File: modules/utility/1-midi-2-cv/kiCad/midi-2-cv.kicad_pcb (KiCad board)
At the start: 2 copper layers, 101 x 110 mm, 163 parts, among them J1 DIN-6, Q1 BC848, Q2 BC848, Q3 BC848, Q4 BC848, SW1 ON-OFF-ON, U1 6N135, U10 MCP4728, U2 YAAJ_WeAct_BlackPill_Part_Like, U3 MCP4728, U4 TL074, U5 MCP4728, U6 TL074, U7 L7805, U8 TL074, U9 TL074

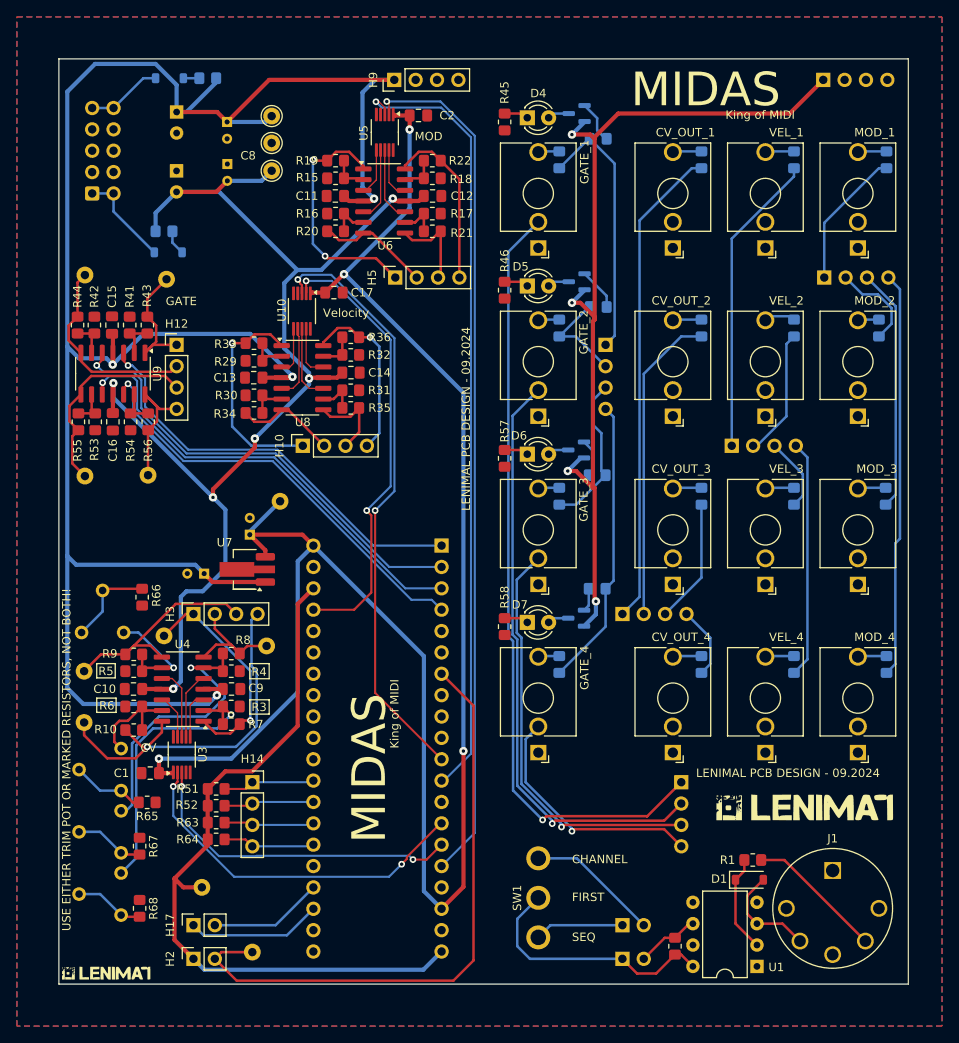
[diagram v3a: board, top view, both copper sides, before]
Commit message: Midi 2 CV (Midas) Rework; Delay (Richochet) Rework. Programming, backups for WeAct CV
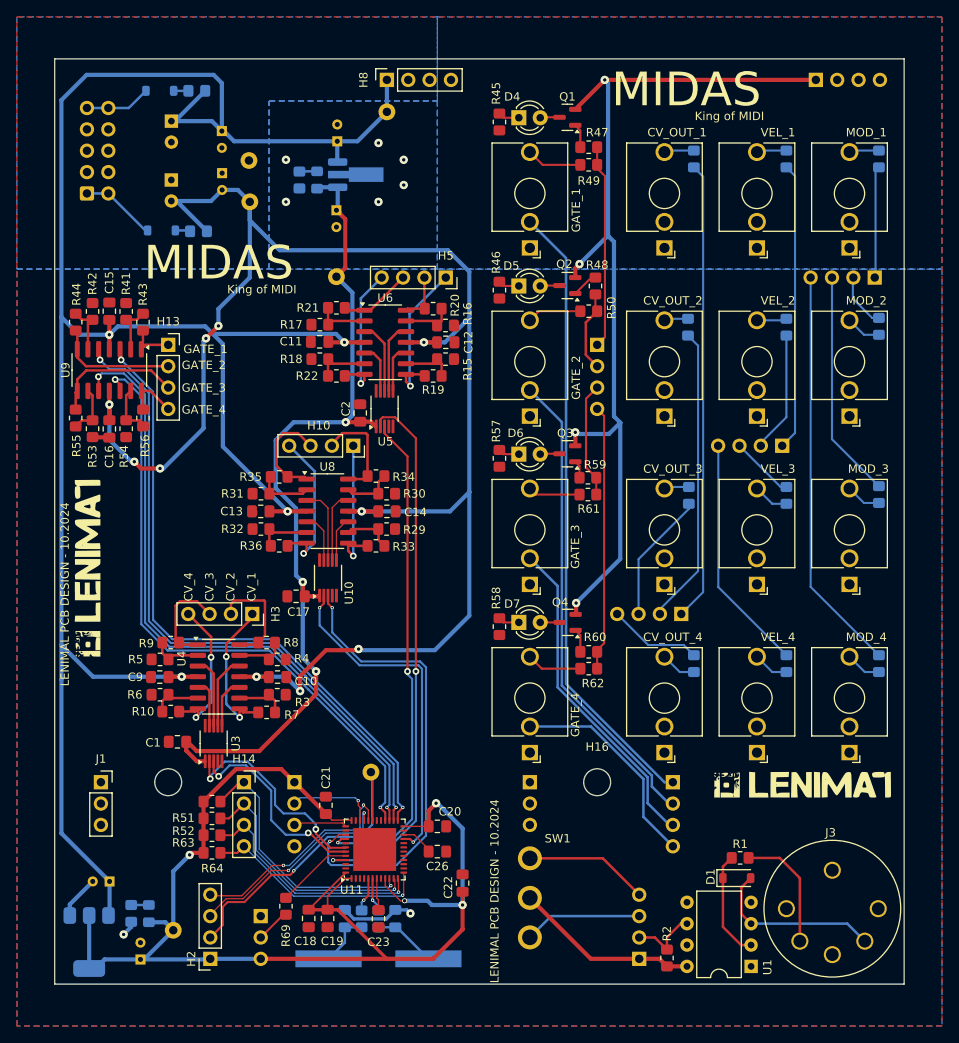
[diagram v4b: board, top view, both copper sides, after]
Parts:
- removed the G*** at (138.8, 139.0)
- removed the G*** at (55.7, 158.7)
- removed the G*** at (55.6, 158.7)
- removed the G*** at (138.6, 139.0)
- removed R65, R66, R67, R68: 6K8, Resistor_SMD:R_0805_2012Metric_Pad1.20x1.40mm_HandSolder
- removed RV1, RV2, RV3, RV4: 20K, Potentiometer_THT:Potentiometer_Piher_PT-6-V_Vertical
- removed TP10: GATE_1_OUT, Connector_Pin:Pin_D1.0mm_L10.0mm
- removed TP11: CV_2_OUT, Connector_Pin:Pin_D1.0mm_L10.0mm
- removed TP12: CV_1_OUT, Connector_Pin:Pin_D1.0mm_L10.0mm
- removed TP13: CV_3_OUT, Connector_Pin:Pin_D1.0mm_L10.0mm
- removed TP14: CV_4_OUT, Connector_Pin:Pin_D1.0mm_L10.0mm
- removed TP7: GATE_3_OUT, Connector_Pin:Pin_D1.0mm_L10.0mm
- removed TP8: GATE_4_OUT, Connector_Pin:Pin_D1.0mm_L10.0mm
- removed TP9: GATE_2_OUT, Connector_Pin:Pin_D1.0mm_L10.0mm
- added C18: 100nF, Capacitor_SMD:C_0805_2012Metric_Pad1.18x1.45mm_HandSolder, F.Cu at (79.7, 152.2)
- added C19: 100nF, Capacitor_SMD:C_0805_2012Metric_Pad1.18x1.45mm_HandSolder, F.Cu at (82.0, 152.2)
- added C20: 100nF, Capacitor_SMD:C_0805_2012Metric_Pad1.18x1.45mm_HandSolder, F.Cu at (95.0, 141.2)
- added C21: 100nF, Capacitor_SMD:C_0805_2012Metric_Pad1.18x1.45mm_HandSolder, F.Cu at (81.8, 138.8)
- added C22: 10uF, Capacitor_SMD:C_0805_2012Metric_Pad1.18x1.45mm_HandSolder, F.Cu at (98.0, 148.0)
- added C23: 100nF, Capacitor_SMD:C_0805_2012Metric_Pad1.18x1.45mm_HandSolder, F.Cu at (88.0, 152.2)
- added C24: 10pF, Capacitor_SMD:C_0805_2012Metric_Pad1.18x1.45mm_HandSolder, B.Cu at (90.0, 152.2)
- added C25: 10pF, Capacitor_SMD:C_0805_2012Metric_Pad1.18x1.45mm_HandSolder, B.Cu at (84.0, 152.2)
- added C26: 2.2uF, Capacitor_SMD:C_0805_2012Metric_Pad1.18x1.45mm_HandSolder, F.Cu at (95.0, 144.2)
- added C27: 10uF, Capacitor_THT:CP_Radial_D4.0mm_P2.00mm, B.Cu at (56.0, 147.8)
- added C28: 10uF, Capacitor_THT:CP_Radial_D4.0mm_P2.00mm, B.Cu at (59.7, 157.1)
- added D8: LED, LED_SMD:LED_0805_2012Metric_Pad1.15x1.40mm_HandSolder, B.Cu at (80.7, 64.4)
- added D9: LED, LED_SMD:LED_0805_2012Metric_Pad1.15x1.40mm_HandSolder, B.Cu at (60.7, 151.6)
- added G***: LOGO, Synth:lenimal_logo_full, F.Cu at (53.4, 110.5)
- added G***: LOGO, Synth:lenimal_logo_full, F.Cu at (138.5, 136.3)
- added G***: LOGO, Synth:lenimal_logo_full, B.Cu at (53.3, 110.4)
- added G***: LOGO, Synth:lenimal_logo_full, B.Cu at (138.6, 136.2)
- added H18: PinHeader_01x04, Synth:PinHeader_1x04_P2.54mm_Vertical, B.Cu at (78.0, 136.0)
- added J2: BOOT_RUN, Connector_PinHeader_2.54mm:PinHeader_1x03_P2.54mm_Vertical, B.Cu at (74.0, 151.9)
- added J3: CONN6_SD-50BV_CUD, Synth:SD-50BV (DIN5), F.Cu at (142.0, 151.0)
- added J4: Conn_01x03, Connector_PinHeader_2.54mm:PinHeader_1x03_P2.54mm_Vertical, B.Cu at (106.0, 136.0)
- added R69: 10K, Resistor_SMD:R_0805_2012Metric_Pad1.20x1.40mm_HandSolder, F.Cu at (77.0, 150.8)
- added R70: 2K, Resistor_SMD:R_0805_2012Metric_Pad1.20x1.40mm_HandSolder, B.Cu at (78.6, 64.4)
- added R71: 2K, Resistor_SMD:R_0805_2012Metric_Pad1.20x1.40mm_HandSolder, B.Cu at (58.6, 151.6)
- added R72: 10R, Resistor_SMD:R_0805_2012Metric_Pad1.20x1.40mm_HandSolder, B.Cu at (86.0, 152.2)
- added R73: 10R, Resistor_SMD:R_0805_2012Metric_Pad1.20x1.40mm_HandSolder, B.Cu at (88.0, 152.2)
- added U11: STM32F401CCUx, Package_DFN_QFN:QFN-48-1EP_7x7mm_P0.5mm_EP5.1x5.1mm, F.Cu at (87.5, 144.0)
- added Y1: 20MHZ, Crystal:Crystal_SMD_HC49-SD_HandSoldering, B.Cu at (88.0, 157.0)
- C3, C6: value 0.1uF -> 10uF
- H1: value PinHeader_01x02 -> PinHeader_01x04; footprint Synth:PinHeader_1x02_P2.54mm_Vertical -> Synth:PinHeader_1x04_P2.54mm_Vertical
- H12, H9, TP1, TP2, TP3: moved to B.Cu
- H13, H8, Q1, Q2, Q3, Q4, R47, R48, R49, R50, R59, R60, R61, R62: moved to F.Cu
- H16: value PinHeader_01x02 -> MountingHole; footprint Synth:PinHeader_1x02_P2.54mm_Vertical -> MountingHole:MountingHole_3.2mm_M3; moved to F.Cu
- H17: value PinSocket_01x02 -> MountingHole; footprint Synth:PinSocket_1x02_P2.54mm_Vertical -> MountingHole:MountingHole_3.2mm_M3
- H2: value PinSocket_01x02 -> PinSocket_01x04; footprint Synth:PinSocket_1x02_P2.54mm_Vertical -> Synth:PinSocket_1x04_P2.54mm_Vertical
- J1: value DIN-6 -> Conn_01x03; footprint Synth:MIDI_DIN5-SD-60BV -> Connector_PinSocket_2.54mm:PinSocket_1x03_P2.54mm_Vertical
- U2: value YAAJ_WeAct_BlackPill_Part_Like -> L78L05_SOT89; footprint stm32:YAAJ_WeAct_BlackPill_2 -> Package_TO_SOT_SMD:SOT-89-3_Handsoldering
- U7: value L7805 -> AMS1117-3.3; footprint Package_TO_SOT_SMD:SOT-89-3_Handsoldering -> Package_TO_SOT_SMD:SOT-223-3_TabPin2; moved to B.Cu
- moved J1 88.3 mm to (55.0, 136.0)
- moved C3 53.8 mm to (83.1, 59.8), turned to 90 degrees
- moved H13 52.0 mm to (63.0, 84.0), turned to 0 degrees
- moved H8 51.9 mm to (89.0, 52.5), turned to 90 degrees
- moved H9 50.1 mm to (140.0, 52.5), turned to -90 degrees
- moved H12 50.0 mm to (114.0, 84.0), turned to 180 degrees
- moved U7 48.0 mm to (53.6, 155.0), turned to -90 degrees
- moved U2 45.2 mm to (85.6, 63.8), turned to 0 degrees
- moved C6 39.9 mm to (83.0, 68.0), turned to -90 degrees
- moved C17 36.4 mm to (78.2, 113.9), turned to 0 degrees
- moved C2 36.0 mm to (85.8, 92.1), turned to -90 degrees
- moved U5 32.9 mm to (88.7, 91.6), turned to 90 degrees
- moved U10 31.9 mm to (82.0, 111.7), turned to 90 degrees
- moved R33 28.1 mm to (87.7, 107.9)
- moved R19 28.1 mm to (94.5, 87.7)
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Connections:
- H14 pad 1: /gate_out/GATE_1_CALLBACK -> /PA0
- H14 pad 2: /gate_out/GATE_2_CALLBACK -> /PA1
- H14 pad 3: /gate_out/GATE_3_CALLBACK -> /PA2
- H14 pad 4: /gate_out/GATE_4_CALLBACK -> /PA3
- H2 pad 2: Net-(H2B-Pin_2) -> /RX
- J1 pad 1: unconnected-(J1-Pad1) -> GNDREF
- J1 pad 2: Net-(J1-Pad2) -> GNDREF
- R1 pad 2: Net-(J1-Pad2) -> Net-(J3-Pad2)
- R10 pad 1: Net-(U4D--) -> Net-(U4B--)
- R15 pad 2: Net-(U6A--) -> Net-(U6C--)
- R16 pad 2: Net-(U6B--) -> Net-(U6D--)
- R17 pad 2: Net-(U6C--) -> Net-(U6A--)
- R18 pad 2: Net-(U6D--) -> Net-(U6B--)
- R19 pad 1: Net-(U6A--) -> Net-(U6C--)
- R20 pad 1: Net-(U6B--) -> Net-(U6D--)
- R21 pad 1: Net-(U6C--) -> Net-(U6A--)
- R22 pad 1: Net-(U6D--) -> Net-(U6B--)
- R29 pad 2: Net-(U8A--) -> Net-(U8C--)
- R3 pad 2: Net-(U4A--) -> Net-(U4C--)
- R30 pad 2: Net-(U8B--) -> Net-(U8D--)
- R31 pad 2: Net-(U8C--) -> Net-(U8A--)
- R32 pad 2: Net-(U8D--) -> Net-(U8B--)
- R33 pad 1: Net-(U8A--) -> Net-(U8C--)
- R34 pad 1: Net-(U8B--) -> Net-(U8D--)
- R35 pad 1: Net-(U8C--) -> Net-(U8A--)
- R36 pad 1: Net-(U8D--) -> Net-(U8B--)
- R4 pad 2: Net-(U4B--) -> Net-(U4D--)
- R43 pad 2: Net-(H12A-Pin_1) -> Net-(H13A-Pin_1)
- R44 pad 2: Net-(H12B-Pin_2) -> Net-(H13B-Pin_2)
- R47 pad 1: Net-(H13A-Pin_1) -> Net-(H12A-Pin_1)
- R48 pad 1: Net-(H13B-Pin_2) -> Net-(H12B-Pin_2)
- R49 pad 1: Net-(H13A-Pin_1) -> Net-(H12A-Pin_1)
- R5 pad 2: Net-(U4C--) -> Net-(U4A--)
- R50 pad 1: Net-(H13B-Pin_2) -> Net-(H12B-Pin_2)
- R51 pad 1: /gate_out/GATE_1_CALLBACK -> /PA0
- R52 pad 1: /gate_out/GATE_2_CALLBACK -> /PA1
- R55 pad 2: Net-(H12C-Pin_3) -> Net-(H13C-Pin_3)
- R56 pad 2: Net-(H12D-Pin_4) -> Net-(H13D-Pin_4)
- R59 pad 1: Net-(H13C-Pin_3) -> Net-(H12C-Pin_3)
- R6 pad 2: Net-(U4D--) -> Net-(U4B--)
- R60 pad 1: Net-(H13D-Pin_4) -> Net-(H12D-Pin_4)
- R61 pad 1: Net-(H13C-Pin_3) -> Net-(H12C-Pin_3)
- R62 pad 1: Net-(H13D-Pin_4) -> Net-(H12D-Pin_4)
- R63 pad 1: /gate_out/GATE_3_CALLBACK -> /PA2
- R64 pad 1: /gate_out/GATE_4_CALLBACK -> /PA3
- R7 pad 1: Net-(U4A--) -> Net-(U4C--)
- R8 pad 1: Net-(U4B--) -> Net-(U4D--)
- R9 pad 1: Net-(U4C--) -> Net-(U4A--)
- SW1 pad 1: Net-(H16A-Pin_1) -> Net-(H1C-Pin_3)
- SW1 pad 3: Net-(H16B-Pin_2) -> Net-(H1D-Pin_4)
- TP6 pad 1: Net-(H2B-Pin_2) -> /RX
- U10 pad 2: /mcp4728_velocity-out/SCL -> /PB10-vel-scl
- U10 pad 3: /mcp4728_velocity-out/SDA -> /PB3-vel-sda
- U2 pad 1: /gate_out/GATE_IN_1 -> +5V
- U2 pad 2: /gate_out/GATE_IN_2 -> GNDREF
- U2 pad 3: /gate_out/GATE_IN_3 -> +12V
- U3 pad 2: /mcp4728_cv-out/SCL -> /PB6-cv-scl
- U3 pad 3: /mcp4728_cv-out/SDA -> /PB7-cv-sda
- U4 pad 1: Net-(H3A-Pin_1) -> Net-(H3C-Pin_3)
- U4 pad 10: Net-(U3-VOUTC) -> Net-(U3-VOUTA)
- U4 pad 12: Net-(U3-VOUTD) -> Net-(U3-VOUTB)
- U4 pad 14: Net-(H3D-Pin_4) -> Net-(H3B-Pin_2)
- U4 pad 3: Net-(U3-VOUTA) -> Net-(U3-VOUTC)
- U4 pad 5: Net-(U3-VOUTB) -> Net-(U3-VOUTD)
- U4 pad 7: Net-(H3B-Pin_2) -> Net-(H3D-Pin_4)
- U4 pad 8: Net-(H3C-Pin_3) -> Net-(H3A-Pin_1)
- U5 pad 2: /mcp4728_mod-wheel-out/SCL -> /PB8-mod-scl
- U5 pad 3: /mcp4728_mod-wheel-out/SDA -> /PB4-mod-sda
- U6 pad 1: Net-(H5A-Pin_1) -> Net-(H5C-Pin_3)
- U6 pad 10: Net-(U5-VOUTC) -> Net-(U5-VOUTA)
- U6 pad 12: Net-(U5-VOUTD) -> Net-(U5-VOUTB)
- U6 pad 14: Net-(H5D-Pin_4) -> Net-(H5B-Pin_2)
- U6 pad 3: Net-(U5-VOUTA) -> Net-(U5-VOUTC)
- U6 pad 5: Net-(U5-VOUTB) -> Net-(U5-VOUTD)
- U6 pad 7: Net-(H5B-Pin_2) -> Net-(H5D-Pin_4)
- U6 pad 8: Net-(H5C-Pin_3) -> Net-(H5A-Pin_1)
- U7 pad 1: +12V -> GNDREF
- U7 pad 2: GNDREF -> +3.3V
- U7 pad 3: +5V -> +12V
- U8 pad 1: Net-(H10A-Pin_1) -> Net-(H10C-Pin_3)
- U8 pad 10: Net-(U10-VOUTC) -> Net-(U10-VOUTA)
- U8 pad 12: Net-(U10-VOUTD) -> Net-(U10-VOUTB)
- U8 pad 14: Net-(H10D-Pin_4) -> Net-(H10B-Pin_2)
- U8 pad 3: Net-(U10-VOUTA) -> Net-(U10-VOUTC)
- U8 pad 5: Net-(U10-VOUTB) -> Net-(U10-VOUTD)
- U8 pad 7: Net-(H10B-Pin_2) -> Net-(H10D-Pin_4)
- U8 pad 8: Net-(H10C-Pin_3) -> Net-(H10A-Pin_1)
- U9 pad 1: Net-(H12A-Pin_1) -> Net-(H13A-Pin_1)
- U9 pad 14: Net-(H12D-Pin_4) -> Net-(H13D-Pin_4)
- U9 pad 7: Net-(H12B-Pin_2) -> Net-(H13B-Pin_2)
- U9 pad 8: Net-(H12C-Pin_3) -> Net-(H13C-Pin_3)
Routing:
- net +5V: track 219.0 -> 103.7 mm, vias 4 -> 3
- net /mcp4728_mod-wheel-out/SCL: track 102.3 -> 0.00 mm, vias 1 -> 0
- net /mcp4728_mod-wheel-out/SDA: track 93.0 -> 0.00 mm, vias 1 -> 0
- net Net-(H2B-Pin_2): track 73.3 -> 0.00 mm
- net /mcp4728_velocity-out/SDA: track 71.0 -> 0.00 mm, vias 2 -> 0
- net /PB8-mod-scl: track 0.00 -> 65.0 mm, vias 0 -> 2
- net +3.3V: track 118.8 -> 181.0 mm, vias 0 -> 4
- net /PB4-mod-sda: track 0.00 -> 59.2 mm, vias 0 -> 2
- net /PB3-vel-sda: track 0.00 -> 55.5 mm, vias 0 -> 2
- net -12V: track 145.9 -> 201.4 mm, vias 6 -> 10
- net /mcp4728_velocity-out/SCL: track 53.6 -> 0.00 mm, vias 2 -> 0
- net /mcp4728_cv-out/SCL: track 43.1 -> 0.00 mm, vias 2 -> 0
- net /PB10-vel-scl: track 0.00 -> 40.4 mm, vias 0 -> 2
- net /mcp4728_cv-out/SDA: track 39.2 -> 0.00 mm, vias 2 -> 0
- net /RX: track 0.00 -> 38.2 mm, vias 0 -> 1
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- added copper zone on B.Cu, net GNDREF
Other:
- board text added: "3.3V"
- board text added: "CV_1"
- board text added: "CV_2"
- board text added: "CV_3"
- board text added: "CV_4"
- board text added: "GATE_1"
- board text added: "GATE_2"
- board text added: "GATE_3"
- board text added: "GATE_4"
- board text added: "LENIMAL PCB DESIGN - 10.2024"
- board text added: "Mod wheel"
- board text added: "PROG"
- board text added: "RUN"
- board text added: "SWD_CLK"
- board text added: "SWD_IO"
- board text removed: "CH.1"
- board text removed: "CH.2"
- board text removed: "CH.3"
- board text removed: "CH.4"
- board text removed: "CHANNEL"
- board text removed: "CV"
- board text removed: "Channel 1"
- board text removed: "Channel 2"
- board text removed: "Channel 3"
- board text removed: "Channel 4"
- board text removed: "FIRST"
- board text removed: "GATE"
- board text removed: "GATE.1"
- board text removed: "GATE.2"
- board text removed: "GATE.3"
- board text removed: "GATE.4"
- board text removed: "LENIMAL PCB DESIGN - 09.2024"
- board text removed: "MIDI_IN"
- board text removed: "MOD"
- board text removed: "SEQ"
- board text removed: "USB SIDE"
- board text removed: "USE EITHER TRIM POT OR MARKED RESISTORS, NOT BOTH!"

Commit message: finish up PCB finals for run-2, continue on C code for midas/sequencer
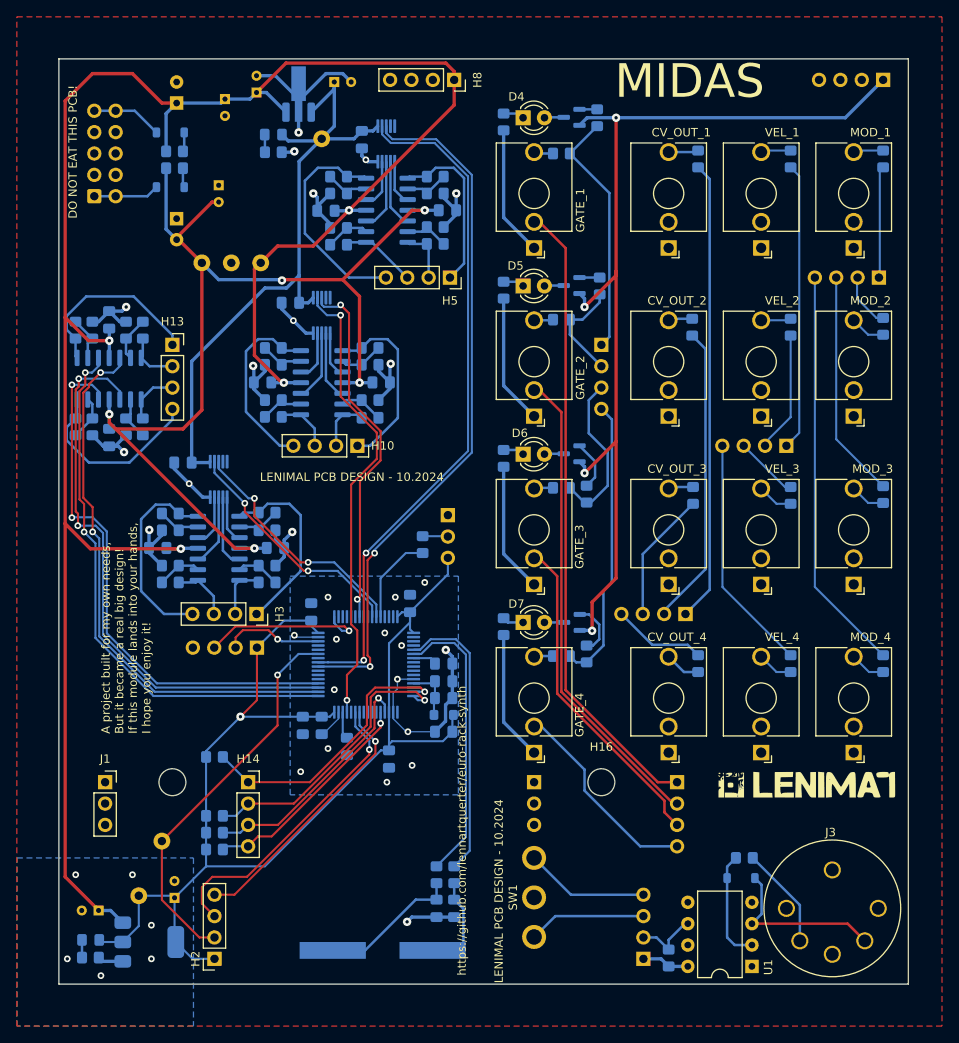
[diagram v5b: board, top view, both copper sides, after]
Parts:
- removed C18, C19, C20, C21, C23: 100nF, Capacitor_SMD:C_0805_2012Metric_Pad1.18x1.45mm_HandSolder
- removed C22: 10uF, Capacitor_SMD:C_0805_2012Metric_Pad1.18x1.45mm_HandSolder
- removed C24, C25: 10pF, Capacitor_SMD:C_0805_2012Metric_Pad1.18x1.45mm_HandSolder
- removed C26: 2.2uF, Capacitor_SMD:C_0805_2012Metric_Pad1.18x1.45mm_HandSolder
- removed the G*** at (53.4, 110.5)
- removed the G*** at (53.3, 110.4)
- removed H18: PinHeader_01x04, Synth:PinHeader_1x04_P2.54mm_Vertical
- removed J2: BOOT_RUN, Connector_PinHeader_2.54mm:PinHeader_1x03_P2.54mm_Vertical
- removed R69: 10K, Resistor_SMD:R_0805_2012Metric_Pad1.20x1.40mm_HandSolder
- removed R72, R73: 10R, Resistor_SMD:R_0805_2012Metric_Pad1.20x1.40mm_HandSolder
- removed Y1: 20MHZ, Crystal:Crystal_SMD_HC49-SD_HandSoldering
- added C29: 100nF, Capacitor_SMD:C_0805_2012Metric_Pad1.18x1.45mm_HandSolder, B.Cu at (81.2, 129.2)
- added C30: 100nF, Capacitor_SMD:C_0805_2012Metric_Pad1.18x1.45mm_HandSolder, B.Cu at (80.0, 115.8)
- added C31: 100nF, Capacitor_SMD:C_0805_2012Metric_Pad1.18x1.45mm_HandSolder, B.Cu at (89.2, 133.2)
- added C32: 100nF, Capacitor_SMD:C_0805_2012Metric_Pad1.18x1.45mm_HandSolder, B.Cu at (91.8, 114.8)
- added C33: 10uF, Capacitor_SMD:C_0805_2012Metric_Pad1.18x1.45mm_HandSolder, B.Cu at (79.0, 129.2)
- added C34: 100nF, Capacitor_SMD:C_0805_2012Metric_Pad1.18x1.45mm_HandSolder, B.Cu at (95.8, 121.9)
- added C35: 10nF, Capacitor_SMD:C_0805_2012Metric_Pad1.18x1.45mm_HandSolder, B.Cu at (95.8, 124.0)
- added C36: 1uF, Capacitor_SMD:C_0805_2012Metric_Pad1.18x1.45mm_HandSolder, B.Cu at (95.8, 126.0)
- added C37: 1uF, Capacitor_SMD:C_0805_2012Metric_Pad1.18x1.45mm_HandSolder, B.Cu at (95.8, 130.0)
- added C38: 10pF, Capacitor_SMD:C_0805_2012Metric_Pad1.18x1.45mm_HandSolder, B.Cu at (97.0, 151.0)
- added C39: 10pF, Capacitor_SMD:C_0805_2012Metric_Pad1.18x1.45mm_HandSolder, B.Cu at (94.9, 151.0)
- added C40: 2.2uF, Capacitor_SMD:C_0805_2012Metric_Pad1.18x1.45mm_HandSolder, B.Cu at (84.2, 131.8)
- added FB1: 120R, Inductor_SMD:L_0805_2012Metric_Pad1.05x1.20mm_HandSolder, B.Cu at (95.8, 128.0)
- added G***: LOGO, Synth:lenimal_logo_full, B.Cu at (86.0, 139.5)
- added J5: BOOT_RUN, Connector_PinHeader_2.54mm:PinHeader_1x03_P2.54mm_Vertical, B.Cu at (96.2, 104.2)
- added J6: Conn_01x04, Connector_PinHeader_2.54mm:PinHeader_1x04_P2.54mm_Vertical, B.Cu at (73.5, 120.0)
- added R65: 10K, Resistor_SMD:R_0805_2012Metric_Pad1.20x1.40mm_HandSolder, B.Cu at (93.2, 107.8)
- added R66: 10R, Resistor_SMD:R_0805_2012Metric_Pad1.20x1.40mm_HandSolder, B.Cu at (97.0, 147.0)
- added R67: 10R, Resistor_SMD:R_0805_2012Metric_Pad1.20x1.40mm_HandSolder, B.Cu at (94.9, 147.0)
- added Y2: 20MHZ, Crystal:Crystal_SMD_HC49-SD_HandSoldering, B.Cu at (88.5, 156.0)
- C1, C10, C11, C12, C13, C14, C15, C16, C17, C2, C9, D1, Q1, Q2, Q3, Q4, R1, R2, R3, R4, R41, R42, R43, R44, R45, R46, R47, R48, R49, R5, R50, R51, R52, R53, R54, R55, R56, R57, R58, R59, R6, R60, R61, R62, R63, R64, U10, U3, U5: moved to B.Cu
- J3: value CONN6_SD-50BV_CUD -> SD-50BV (DIN5)
- R10, R7, R8, R9: value 47K [0.1%] -> 30K [0.1%]; moved to B.Cu
- R15, R16, R17, R18, R29, R30, R31, R32: value 10K [1%] -> 10K [0.1%]; moved to B.Cu
- R19, R20, R21, R22, R33, R34, R35, R36: value 47K [1%] -> 30K [0.1%]; moved to B.Cu
- U11: value STM32F401CCUx -> STM32F411RETx; footprint Package_DFN_QFN:QFN-48-1EP_7x7mm_P0.5mm_EP5.1x5.1mm -> Package_QFP:LQFP-64_10x10mm_P0.5mm; moved to B.Cu
- U4, U6, U8, U9: footprint Package_SO:SOIC-14_3.9x8.7mm_P1.27mm -> Synth:SOIC-14; moved to B.Cu
- moved C17 34.9 mm to (77.5, 79.0)
- moved C1 33.2 mm to (64.8, 98.0)
- moved C2 32.5 mm to (86.0, 59.6), turned to 90 degrees
- moved U5 31.5 mm to (88.9, 60.1), turned to -90 degrees
- moved U3 31.4 mm to (69.0, 100.0), turned to -90 degrees
- moved U10 31.2 mm to (81.2, 80.5), turned to -90 degrees
- moved TP6 26.2 mm to (62.2, 143.0)
- moved R7 23.8 mm to (74.8, 104.0)
- moved R19 23.7 mm to (94.8, 64.0)
- moved R22 23.7 mm to (83.2, 64.0)
- moved R10 23.6 mm to (63.2, 104.0)
- moved R33 23.5 mm to (87.0, 84.4)
- moved R36 23.5 mm to (75.5, 84.4)
- moved TP2 23.4 mm to (74.0, 74.2), turned to 180 degrees
- moved U11 22.0 mm to (86.5, 122.0), turned to 180 degrees
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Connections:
- net /PB4-mod-sda renamed /STM32F411RE/MOD_SDA
- H14 pad 1: /PA0 -> /STM32F411RE/GATE_1_IN
- H14 pad 2: /PA1 -> /STM32F411RE/GATE_2_IN
- H14 pad 3: /PA2 -> /STM32F411RE/GATE_3_IN
- H14 pad 4: /PA3 -> /STM32F411RE/GATE_4_IN
- H2 pad 2: /RX -> /STM32F411RE/MIDI_IN
- H2 pad 3: /MODE_1 -> /STM32F411RE/MODE_SW_1
- H2 pad 4: /MODE_2 -> /STM32F411RE/MODE_SW_2
- R51 pad 1: /PA0 -> /STM32F411RE/GATE_1_IN
- R52 pad 1: /PA1 -> /STM32F411RE/GATE_2_IN
- R63 pad 1: /PA2 -> /STM32F411RE/GATE_3_IN
- R64 pad 1: /PA3 -> /STM32F411RE/GATE_4_IN
- SW1 pad 2: +3.3V -> GNDREF
- TP6 pad 1: /RX -> /STM32F411RE/MIDI_IN
- U10 pad 2: /PB10-vel-scl -> /STM32F411RE/VEL_SCL
- U10 pad 3: /PB3-vel-sda -> /STM32F411RE/VEL_SDA
- U11 pad 10: /PA0 -> unconnected-(U11-PC2-Pad10)
- U11 pad 11: /PA1 -> unconnected-(U11-PC3-Pad11)
- U11 pad 12: /PA2 -> GNDREF
- U11 pad 13: /PA3 -> +3.3VA
- U11 pad 15: unconnected-(U11-PA5-Pad15) -> /STM32F411RE/GATE_1_IN
- U11 pad 16: unconnected-(U11-PA6-Pad16) -> /STM32F411RE/GATE_2_IN
- U11 pad 18: unconnected-(U11-PB0-Pad18) -> GNDREF
- U11 pad 19: unconnected-(U11-PB1-Pad19) -> +3.3V
- U11 pad 20: unconnected-(U11-PB2-Pad20) -> /STM32F411RE/GATE_3_IN
- U11 pad 21: /PB10-vel-scl -> /STM32F411RE/GATE_4_IN
- U11 pad 22: /VCap -> unconnected-(U11-PA6-Pad22)
- U11 pad 23: GNDREF -> unconnected-(U11-PA7-Pad23)
- U11 pad 24: +3.3V -> unconnected-(U11-PC4-Pad24)
- U11 pad 25: /gate_out/GATE_IN_1 -> unconnected-(U11-PC5-Pad25)
- U11 pad 26: /gate_out/GATE_IN_2 -> /STM32F411RE/MODE_SW_2
- U11 pad 27: /gate_out/GATE_IN_3 -> /STM32F411RE/MODE_SW_1
- U11 pad 28: /gate_out/GATE_IN_4 -> unconnected-(U11-PB2-Pad28)
- U11 pad 29: unconnected-(U11-PA8-Pad29) -> /STM32F411RE/VEL_SCL
- U11 pad 30: unconnected-(U11-PA9-Pad30) -> /STM32F411RE/VCap
- U11 pad 31: /RX -> GNDREF
- U11 pad 32: /MODE_2 -> +3.3V
- U11 pad 33: /MODE_1 -> /STM32F411RE/GATE_1_OUT
- U11 pad 34: /SWD_IO -> /STM32F411RE/GATE_2_OUT
- U11 pad 35: GNDREF -> /STM32F411RE/GATE_3_OUT
- U11 pad 36: +3.3V -> /STM32F411RE/GATE_4_OUT
- U11 pad 37: /SWD_CLK -> unconnected-(U11-PC6-Pad37)
- U11 pad 39: /PB3-vel-sda -> unconnected-(U11-PC8-Pad39)
- U11 pad 41: unconnected-(U11-PB5-Pad41) -> /STM32F411RE/MOD_SCL
- U11 pad 42: /PB6-cv-scl -> unconnected-(U11-PA9-Pad42)
- U11 pad 43: /PB7-cv-sda -> /STM32F411RE/MIDI_IN
- U11 pad 44: Net-(U11-BOOT0) -> unconnected-(U11-PA11-Pad44)
- U11 pad 45: /PB8-mod-scl -> unconnected-(U11-PA12-Pad45)
- U11 pad 46: unconnected-(U11-PB9-Pad46) -> /STM32F411RE/SWD_IO
- U11 pad 49: GNDREF -> /STM32F411RE/SWD_CLK
- U11 pad 5: /HSC_IN -> /STM32F411RE/HSC_IN
- U11 pad 6: /HSC_OUT -> /STM32F411RE/HSC_OUT
- U11 pad 7: /NRST -> /STM32F411RE/NRST
- U11 pad 8: GNDREF -> unconnected-(U11-PC0-Pad8)
- U11 pad 9: +3.3V -> unconnected-(U11-PC1-Pad9)
- U3 pad 2: /PB6-cv-scl -> /STM32F411RE/CV_SCL
- U3 pad 3: /PB7-cv-sda -> /STM32F411RE/CV_SDA
- U5 pad 2: /PB8-mod-scl -> /STM32F411RE/MOD_SCL
- U9 pad 10: /gate_out/GATE_IN_3 -> /STM32F411RE/GATE_3_OUT
- U9 pad 12: /gate_out/GATE_IN_4 -> /STM32F411RE/GATE_4_OUT
- U9 pad 3: /gate_out/GATE_IN_1 -> /STM32F411RE/GATE_1_OUT
- U9 pad 5: /gate_out/GATE_IN_2 -> /STM32F411RE/GATE_2_OUT
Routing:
- net GNDREF: track 22.3 -> 195.7 mm, vias 8 -> 35
- net /STM32F411RE/MOD_SCL: track 0.00 -> 81.5 mm, vias 0 -> 2
- net /gate_out/GATE_IN_2: track 79.0 -> 0.00 mm, vias 2 -> 0
- net /gate_out/GATE_IN_3: track 78.5 -> 0.00 mm, vias 2 -> 0
- net /gate_out/GATE_IN_1: track 77.3 -> 0.00 mm, vias 2 -> 0
- net /gate_out/GATE_IN_4: track 75.6 -> 0.00 mm, vias 2 -> 0
- net -12V: track 201.4 -> 131.2 mm, vias 10 -> 5
- net /STM32F411RE/GATE_3_OUT: track 0.00 -> 67.9 mm, vias 0 -> 2
- net /STM32F411RE/GATE_2_OUT: track 0.00 -> 65.3 mm, vias 0 -> 2
- net /PB8-mod-scl: track 65.0 -> 0.00 mm, vias 2 -> 0
- net /STM32F411RE/GATE_1_OUT: track 0.00 -> 64.8 mm, vias 0 -> 2
- net /STM32F411RE/GATE_4_OUT: track 0.00 -> 64.8 mm, vias 0 -> 2
- net /PB3-vel-sda: track 55.5 -> 0.00 mm, vias 2 -> 0
- net /STM32F411RE/VEL_SCL: track 0.00 -> 55.2 mm, vias 0 -> 2
- net /STM32F411RE/MIDI_IN: track 0.00 -> 46.4 mm, vias 0 -> 1
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- removed copper zone on B.Cu, net (none)
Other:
- board text added: "20MHZ"
- board text added: "A project built for my own needs, But it became a real big design! If this module lands into your hands, I hope you enjoy it!"
- board text added: "CLK"
- board text added: "DO NOT EAT THIS PCB!"
- board text added: "IO"
- board text added: "MIDI_IN"
- board text added: "PWR_3V"
- board text added: "PWR_5V"
- board text added: "STM32 F411 RET7"
- board text added: "TL074"
- board text added: "https://github.com/lennartquerter/euro-rack-synth"
- board text removed: "3.3V"
- board text removed: "CV_1"
- board text removed: "CV_2"
- board text removed: "CV_3"
- board text removed: "CV_4"
- board text removed: "GATE_1"
- board text removed: "GATE_2"
- board text removed: "GATE_3"
- board text removed: "GATE_4"
- board text removed: "King of MIDI"
- board text removed: "Mod wheel"
- board text removed: "PROG"
- board text removed: "RUN"
- board text removed: "SWD_CLK"
- board text removed: "SWD_IO"
- board text removed: "Velocity"
